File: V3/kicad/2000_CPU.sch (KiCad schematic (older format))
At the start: 18 parts, among them J1 Conn_01x08_Male, U2000 Z8-L180-S180-180-PLCC-68, U2101 GAL16V8, U2102 14.7456 MHz

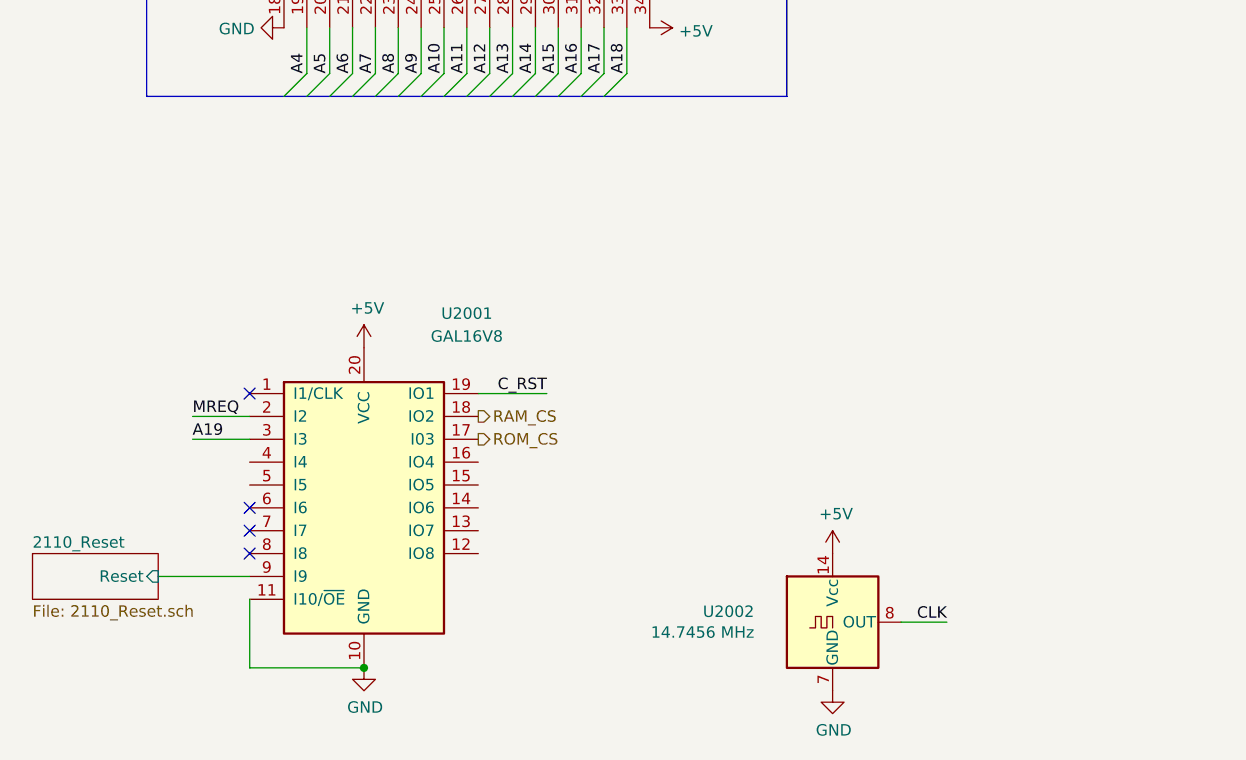
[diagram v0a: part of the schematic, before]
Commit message: Replace reset with simpler circuit
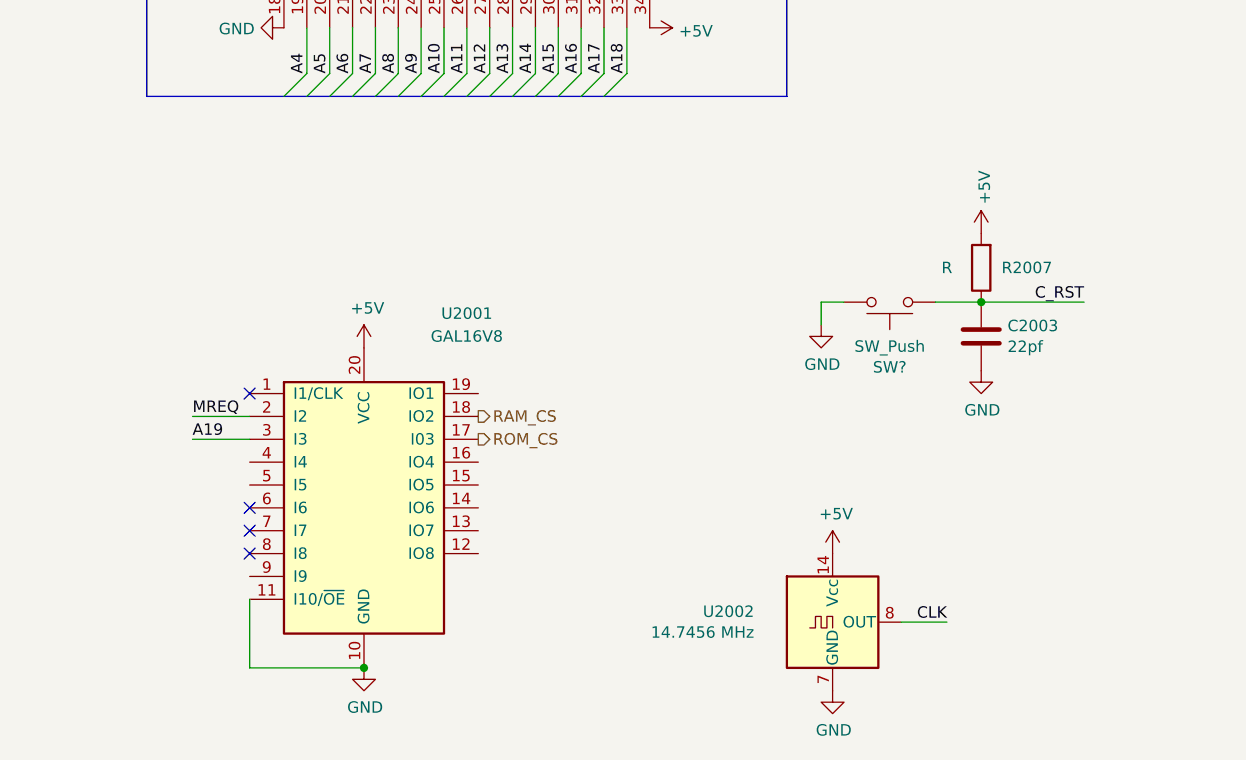
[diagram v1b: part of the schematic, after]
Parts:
- added C2003: 22pf, Capacitor_SMD:C_1206_3216Metric, symbol Device:C
- added R2007: R, Resistor_SMD:R_1206_3216Metric, symbol Device:R
- added SW?: SW_Push, Button_Switch_THT:SW_PUSH_6mm, symbol Switch:SW_Push
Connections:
- net +5V: now also R2007.2
- net C_RST: now also C2003.1, R2007.1, SW?.1; no longer U2101.19 (IO1)
- net GND: now also C2003.2, SW?.2
- net 2110_Reset/Reset: no longer names the net of U2101.9 (I9)
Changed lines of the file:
@@
 $Descr A4 11693 8268
 encoding utf-8
-Sheet 3 5
+Sheet 3 4
 Title ""
 Date ""
@@
 Text HLabel 3300 5700 2    50   Output ~ 0
 RAM_CS
-$Sheet
-S 1350 6300 550  200
-U 62512FB8
-F0 "2110_Reset" 50
-F1 "2110_Reset.sch" 50
-F2 "Reset" I R 1900 6400 50
-$EndSheet
 $Comp
 L Oscillator:ACO-xxxMHz X?
@@
 Text Label 3550 1250 3    50   ~ 0
 CKS
-Text Label 3600 5600 2    50   ~ 0
-C_RST
-Wire Wire Line
-	3300 5600 3600 5600
 $Comp
 L Device:C C?
@@
 Wire Wire Line
 	5150 6600 5350 6600
-Wire Wire Line
-	1900 6400 2300 6400
 Text Label 1950 2200 2    50   ~ 0
 CLK
@@
 Text Label 6750 4750 0    50   ~ 0
 SD_CD
+$Comp
+L Switch:SW_Push SW?
+U 1 1 6545E409
+P 5100 5200
+AR Path="/6545E409" Ref="SW?"  Part="1"
+AR Path="/62497D60/6545E409" Ref="SW?"  Part="1"
+AR Path="/61D852D7/6545E409" Ref="SW?"  Part="1"
+AR Path="/6191B6A2/624CF3AF/6545E409" Ref="SW?"  Part="1"
+AR Path="/6191B6A2/61EBDADB/62512FB8/6545E409" Ref="SW?"  Part="1"
+AR Path="/63A83936/62512FB8/6545E409" Ref="SW?"  Part="1"
+AR Path="/63A83936/6545E409" Ref="SW?"  Part="1"
+F 0 "SW?" H 5100 5485 50  0000 C CNN
+F 1 "SW_Push" H 5100 5394 50  0000 C CNN
+F 2 "Button_Switch_THT:SW_PUSH_6mm" H 5100 5400 50  0001 C CNN
+F 3 "~" H 5100 5400 50  0001 C CNN
+	1    5100 5200
+	-1   0    0    1
+$EndComp
+$Comp
+L Device:R R?
+U 1 1 6546AA6A
+P 5500 5050
+AR Path="/6191B6A2/61EBDADB/6546AA6A" Ref="R?"  Part="1"
+AR Path="/63A83936/6546AA6A" Ref="R2007"  Part="1"
+F 0 "R2007" H 5300 5050 50  0000 C CNN
+F 1 "R" H 5650 5050 50  0000 C CNN
+F 2 "Resistor_SMD:R_1206_3216Metric" V 5430 5050 50  0001 C CNN
+F 3 "~" H 5500 5050 50  0001 C CNN
+	1    5500 5050
+	-1   0    0    1
+$EndComp
+$Comp
+L power:+5V #PWR?
+U 1 1 6546C304
+P 5500 4900
+AR Path="/6191B6A2/61EBDADB/6546C304" Ref="#PWR?"  Part="1"
+AR Path="/63A83936/6546C304" Ref="#PWR?"  Part="1"
+F 0 "#PWR?" H 5500 4750 50  0001 C CNN
+F 1 "+5V" V 5515 5028 50  0000 L CNN
+F 2 "" H 5500 4900 50  0001 C CNN
+F 3 "" H 5500 4900 50  0001 C CNN
+	1    5500 4900
+	1    0    0    -1
+$EndComp
+Text Label 5950 5200 2    50   ~ 0
+C_RST
+Wire Wire Line
+	5500 5200 5950 5200
+Wire Wire Line
+	4900 5200 4800 5200
+Wire Wire Line
+	4800 5200 4800 5300
+$Comp
+L power:GND #PWR?
+U 1 1 6547BF82
+P 4800 5300
+F 0 "#PWR?" H 4800 5050 50  0001 C CNN
+F 1 "GND" H 4805 5127 50  0000 C CNN
+F 2 "" H 4800 5300 50  0001 C CNN
+F 3 "" H 4800 5300 50  0001 C CNN
+	1    4800 5300
+	1    0    0    -1
+$EndComp
+$Comp
+L Device:C C?
+U 1 1 65481B20
+P 5500 5350
+AR Path="/6195D2C9/65481B20" Ref="C?"  Part="1"
+AR Path="/6191B6A2/61F28B7D/65481B20" Ref="C?"  Part="1"
+AR Path="/6191B6A2/61EBDADB/65481B20" Ref="C?"  Part="1"
+AR Path="/63A83936/65481B20" Ref="C2003"  Part="1"
+F 0 "C2003" H 5615 5396 50  0000 L CNN
+F 1 "22pf" H 5615 5305 50  0000 L CNN
+F 2 "Capacitor_SMD:C_1206_3216Metric" H 5538 5200 50  0001 C CNN
+F 3 "~" H 5500 5350 50  0001 C CNN
+	1    5500 5350
+	1    0    0    -1
+$EndComp
+$Comp
+L power:GND #PWR?
+U 1 1 65481B26
+P 5500 5500
+AR Path="/65481B26" Ref="#PWR?"  Part="1"
+AR Path="/62497D60/65481B26" Ref="#PWR?"  Part="1"
+AR Path="/61D852D7/65481B26" Ref="#PWR?"  Part="1"
+AR Path="/6195D2C9/65481B26" Ref="#PWR?"  Part="1"
+AR Path="/6191B6A2/61F28B7D/65481B26" Ref="#PWR?"  Part="1"
+AR Path="/6191B6A2/61EBDADB/65481B26" Ref="#PWR?"  Part="1"
+AR Path="/63A83936/65481B26" Ref="#PWR?"  Part="1"
+F 0 "#PWR?" H 5500 5250 50  0001 C CNN
+F 1 "GND" H 5505 5327 50  0000 C CNN
+F 2 "" H 5500 5500 50  0001 C CNN
+F 3 "" H 5500 5500 50  0001 C CNN
+	1    5500 5500
+	1    0    0    -1
+$EndComp
+Connection ~ 5500 5200
+Wire Wire Line
+	5300 5200 5500 5200
 Wire Bus Line
 	1850 3200 1850 4300

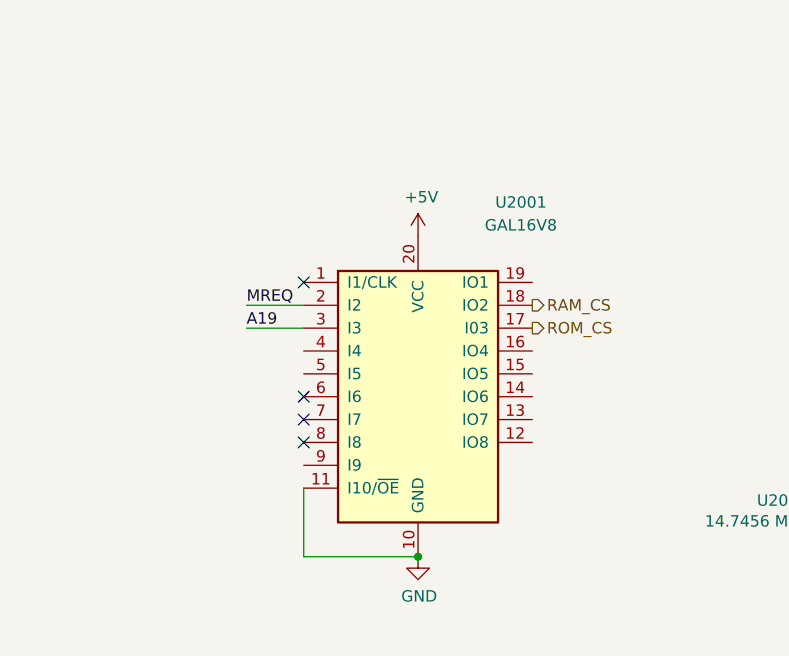
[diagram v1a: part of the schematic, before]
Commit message: replace GAL with 74 series logic
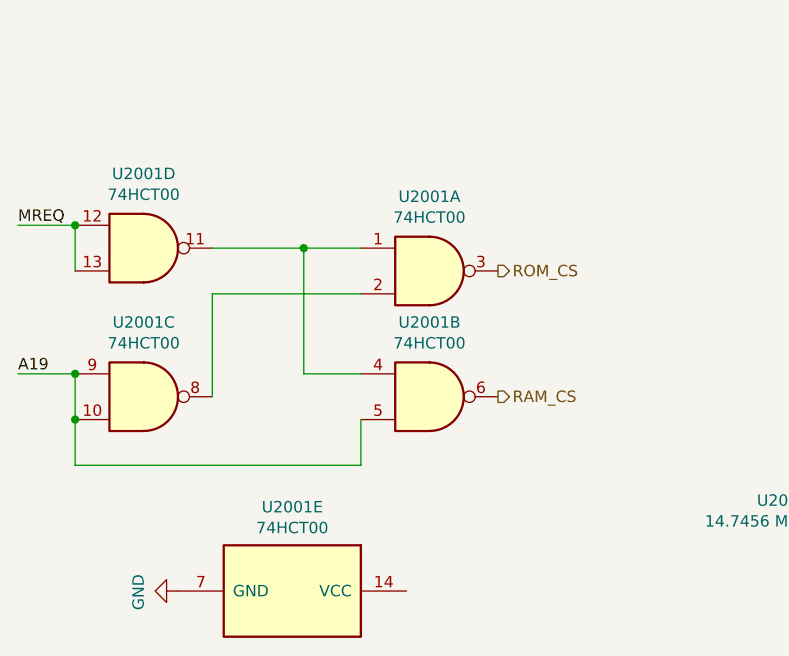
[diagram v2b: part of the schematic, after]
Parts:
- removed U2101: GAL16V8, Package_DIP:DIP-20_W7.62mm_Socket_LongPads, symbol Logic_Programmable:GAL16V8
- added U2001: 74HCT00, symbol 74xx:74HCT00
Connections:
- net A19: now also U2001.10, U2001.5, U2001.9
- net GND: now also U2001.7 (GND)
- net MREQ: now also U2001.12, U2001.13
- net RAM_CS: now also U2001.6
- net ROM_CS: now also U2001.3
- new net: U2001.1, U2001.11, U2001.4
- new net: U2001.2, U2001.8
- no-connect marks 5 -> 1
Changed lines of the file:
@@
 Text Label 4550 3600 2    50   ~ 0
 A19
-$Comp
-L power:GND #PWR?
-U 1 1 624D98DF
-P 2800 6800
-AR Path="/624D98DF" Ref="#PWR?"  Part="1"
-AR Path="/6191B6A2/624D98DF" Ref="#PWR?"  Part="1"
-AR Path="/6191B6A2/61F0BDAE/624D98DF" Ref="#PWR?"  Part="1"
-AR Path="/6195D2C9/624D98DF" Ref="#PWR?"  Part="1"
-AR Path="/6191B6A2/61EBDADB/624D98DF" Ref="#PWR0101"  Part="1"
-AR Path="/63A83936/624D98DF" Ref="#PWR0103"  Part="1"
-F 0 "#PWR0103" H 2800 6550 50  0001 C CNN
-F 1 "GND" H 2805 6627 50  0000 C CNN
-F 2 "" H 2800 6800 50  0001 C CNN
-F 3 "" H 2800 6800 50  0001 C CNN
-	1    2800 6800
-	1    0    0    -1
-$EndComp
-$Comp
-L power:+5V #PWR?
-U 1 1 624D98F5
-P 2800 5400
-AR Path="/6195D2C9/624D98F5" Ref="#PWR?"  Part="1"
-AR Path="/6191B6A2/624D98F5" Ref="#PWR?"  Part="1"
-AR Path="/6191B6A2/61EBDADB/624D98F5" Ref="#PWR0102"  Part="1"
-AR Path="/63A83936/624D98F5" Ref="#PWR0104"  Part="1"
-F 0 "#PWR0104" H 2800 5250 50  0001 C CNN
-F 1 "+5V" H 2815 5573 50  0000 C CNN
-F 2 "" H 2800 5400 50  0001 C CNN
-F 3 "" H 2800 5400 50  0001 C CNN
-	1    2800 5400
-	1    0    0    -1
-$EndComp
-Wire Wire Line
-	2300 5700 2050 5700
-Text Label 2050 5700 0    50   ~ 0
+Text Label 1050 5350 0    50   ~ 0
 MREQ
-Text HLabel 3300 5800 2    50   Output ~ 0
+Text HLabel 3150 5550 2    50   Output ~ 0
 ROM_CS
-Text Label 2050 5800 0    50   ~ 0
-A19
-Text HLabel 3300 5700 2    50   Output ~ 0
+Text HLabel 3150 6100 2    50   Output ~ 0
 RAM_CS
 $Comp
@@
 Text Label 2950 1250 3    50   ~ 0
 MREQ
-$Comp
-L Logic_Programmable:GAL16V8 U?
-U 1 1 624D98D9
-P 2800 6100
-AR Path="/624D98D9" Ref="U?"  Part="1"
-AR Path="/6191B6A2/624D98D9" Ref="U?"  Part="1"
-AR Path="/6191B6A2/61F0BDAE/624D98D9" Ref="U?"  Part="1"
-AR Path="/6195D2C9/624D98D9" Ref="U?"  Part="1"
-AR Path="/6191B6A2/61EBDADB/624D98D9" Ref="U2101"  Part="1"
-AR Path="/63A83936/624D98D9" Ref="U2001"  Part="1"
-F 0 "U2001" H 3250 6950 50  0000 C CNN
-F 1 "GAL16V8" H 3250 6850 50  0000 C CNN
-F 2 "Package_DIP:DIP-20_W7.62mm_Socket_LongPads" H 2800 6100 50  0001 C CNN
-F 3 "" H 2800 6100 50  0001 C CNN
-	1    2800 6100
-	1    0    0    -1
-$EndComp
 Wire Wire Line
 	2150 3100 1850 3100
@@
 	1    0    0    -1
 $EndComp
-Wire Wire Line
-	2050 5800 2300 5800
 Text HLabel 4750 3500 2    50   BiDi ~ 0
 D[0..7]
@@
 Text HLabel 2650 1250 1    50   Output ~ 0
 WR
-NoConn ~ 2300 6200
-NoConn ~ 2300 6300
-Wire Wire Line
-	2300 6500 2300 6800
-Wire Wire Line
-	2300 6800 2800 6800
-Connection ~ 2800 6800
 Text Label 4650 2600 2    50   ~ 0
 RTS0
 Wire Wire Line
 	4650 2600 4350 2600
-NoConn ~ 2300 5600
 $Comp
 L Device:LED D2102/ST1
@@
 	0    -1   -1   0
 $EndComp
-NoConn ~ 2300 6100
 Wire Wire Line
 	2150 3200 1950 3200
@@
 Wire Wire Line
 	5300 5200 5500 5200
+$Comp
+L 74xx:74HCT00 U2001
+U 1 1 6548B5B9
+P 2850 5550
+F 0 "U2001" H 2850 5875 50  0000 C CNN
+F 1 "74HCT00" H 2850 5784 50  0000 C CNN
+F 2 "" H 2850 5550 50  0001 C CNN
+F 3 "http://www.ti.com/lit/gpn/sn74hct00" H 2850 5550 50  0001 C CNN
+	1    2850 5550
+	1    0    0    -1
+$EndComp
+$Comp
+L 74xx:74HCT00 U2001
+U 2 1 6548F371
+P 2850 6100
+F 0 "U2001" H 2850 6425 50  0000 C CNN
+F 1 "74HCT00" H 2850 6334 50  0000 C CNN
+F 2 "" H 2850 6100 50  0001 C CNN
+F 3 "http://www.ti.com/lit/gpn/sn74hct00" H 2850 6100 50  0001 C CNN
+	2    2850 6100
+	1    0    0    -1
+$EndComp
+$Comp
+L 74xx:74HCT00 U2001
+U 3 1 65490F1D
+P 1600 6100
+F 0 "U2001" H 1600 6425 50  0000 C CNN
+F 1 "74HCT00" H 1600 6334 50  0000 C CNN
+F 2 "" H 1600 6100 50  0001 C CNN
+F 3 "http://www.ti.com/lit/gpn/sn74hct00" H 1600 6100 50  0001 C CNN
+	3    1600 6100
+	1    0    0    -1
+$EndComp
+$Comp
+L 74xx:74HCT00 U2001
+U 5 1 65493A9A
+P 2250 6950
+F 0 "U2001" V 1883 6950 50  0000 C CNN
+F 1 "74HCT00" V 1974 6950 50  0000 C CNN
+F 2 "" H 2250 6950 50  0001 C CNN
+F 3 "http://www.ti.com/lit/gpn/sn74hct00" H 2250 6950 50  0001 C CNN
+	5    2250 6950
+	0    1    1    0
+$EndComp
+Wire Wire Line
+	1050 6000 1300 6000
+Text Label 1050 6000 0    50   ~ 0
+A19
+Wire Wire Line
+	1300 6000 1300 6200
+Connection ~ 1300 6000
+Wire Wire Line
+	1900 5450 2300 5450
+Wire Wire Line
+	1900 6100 1900 5650
+Wire Wire Line
+	1900 5650 2550 5650
+Wire Wire Line
+	1300 6200 1300 6400
+Wire Wire Line
+	1300 6400 2550 6400
+Wire Wire Line
+	2550 6400 2550 6200
+Connection ~ 1300 6200
+Wire Wire Line
+	2300 5450 2300 6000
+Wire Wire Line
+	2300 6000 2550 6000
+Connection ~ 2300 5450
+Wire Wire Line
+	2300 5450 2550 5450
+$Comp
+L power:GND #PWR?
+U 1 1 654D56A5
+P 1750 6950
+AR Path="/654D56A5" Ref="#PWR?"  Part="1"
+AR Path="/62497D60/654D56A5" Ref="#PWR?"  Part="1"
+AR Path="/61D852D7/654D56A5" Ref="#PWR?"  Part="1"
+AR Path="/6195D2C9/654D56A5" Ref="#PWR?"  Part="1"
+AR Path="/6191B6A2/61F28B7D/654D56A5" Ref="#PWR?"  Part="1"
+AR Path="/6191B6A2/61EBDADB/654D56A5" Ref="#PWR?"  Part="1"
+AR Path="/63A83936/654D56A5" Ref="#PWR?"  Part="1"
+F 0 "#PWR?" H 1750 6700 50  0001 C CNN
+F 1 "GND" H 1755 6777 50  0000 C CNN
+F 2 "" H 1750 6950 50  0001 C CNN
+F 3 "" H 1750 6950 50  0001 C CNN
+	1    1750 6950
+	0    1    1    0
+$EndComp
+Connection ~ 1300 5350
+Wire Wire Line
+	1300 5350 1300 5550
+$Comp
+L 74xx:74HCT00 U2001
+U 4 1 65492729
+P 1600 5450
+F 0 "U2001" H 1600 5775 50  0000 C CNN
+F 1 "74HCT00" H 1600 5684 50  0000 C CNN
+F 2 "" H 1600 5450 50  0001 C CNN
+F 3 "http://www.ti.com/lit/gpn/sn74hct00" H 1600 5450 50  0001 C CNN
+	4    1600 5450
+	1    0    0    -1
+$EndComp
+Wire Wire Line
+	1300 5350 1050 5350
 Wire Bus Line
 	1850 3200 1850 4300

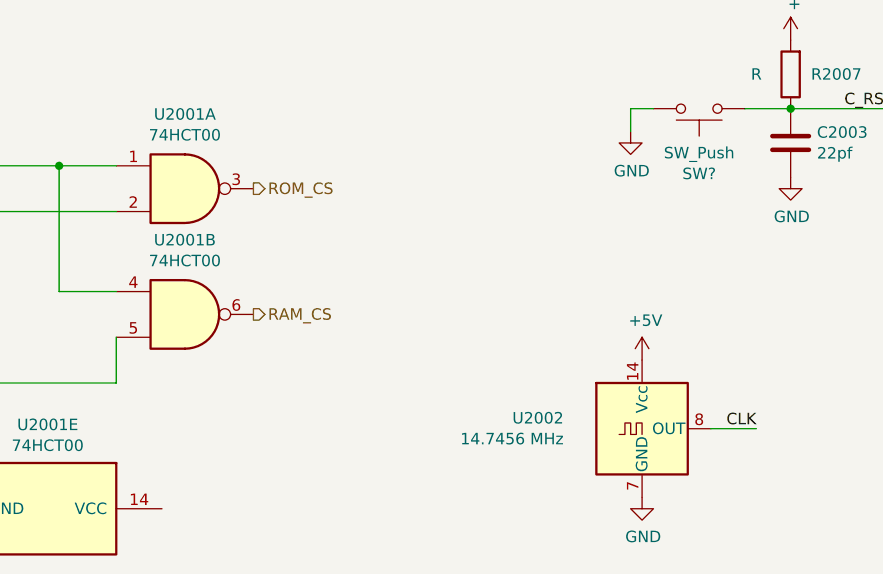
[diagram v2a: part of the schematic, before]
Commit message: rearranged pcb a bit
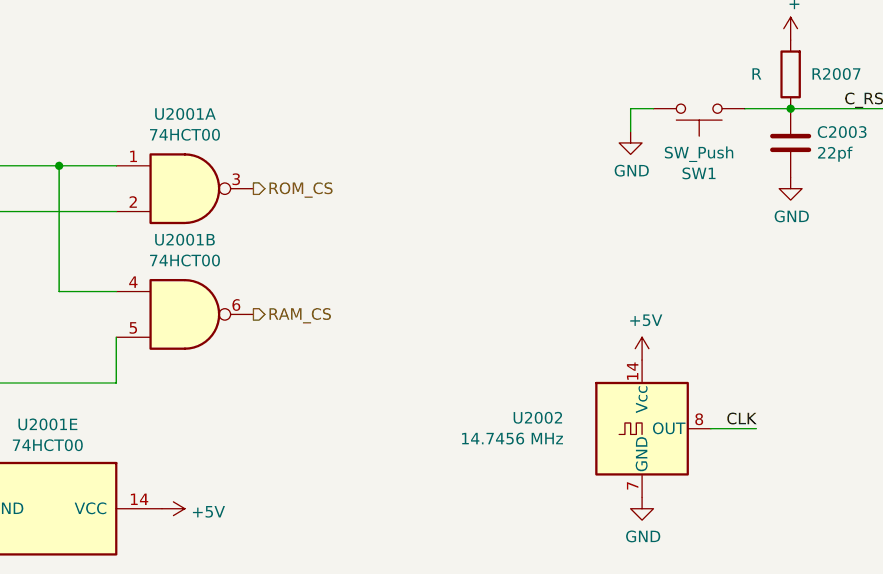
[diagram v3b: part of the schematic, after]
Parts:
- U2001: footprint (none) -> Package_DIP:DIP-14_W7.62mm_Socket_LongPads
- gave numbers to parts that had none: 1
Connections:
- net +5V: now also U2001.14 (VCC)
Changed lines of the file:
@@
 AR Path="/6191B6A2/61EBDADB/62512FB8/6545E409" Ref="SW?"  Part="1"
 AR Path="/63A83936/62512FB8/6545E409" Ref="SW?"  Part="1"
-AR Path="/63A83936/6545E409" Ref="SW?"  Part="1"
-F 0 "SW?" H 5100 5485 50  0000 C CNN
+AR Path="/63A83936/6545E409" Ref="SW1"  Part="1"
+F 0 "SW1" H 5100 5485 50  0000 C CNN
 F 1 "SW_Push" H 5100 5394 50  0000 C CNN
 F 2 "Button_Switch_THT:SW_PUSH_6mm" H 5100 5400 50  0001 C CNN
@@
 P 5500 4900
 AR Path="/6191B6A2/61EBDADB/6546C304" Ref="#PWR?"  Part="1"
-AR Path="/63A83936/6546C304" Ref="#PWR?"  Part="1"
-F 0 "#PWR?" H 5500 4750 50  0001 C CNN
+AR Path="/63A83936/6546C304" Ref="#PWR0103"  Part="1"
+F 0 "#PWR0103" H 5500 4750 50  0001 C CNN
 F 1 "+5V" V 5515 5028 50  0000 L CNN
 F 2 "" H 5500 4900 50  0001 C CNN
@@
 	4800 5200 4800 5300
 $Comp
-L power:GND #PWR?
+L power:GND #PWR0104
 U 1 1 6547BF82
 P 4800 5300
-F 0 "#PWR?" H 4800 5050 50  0001 C CNN
+F 0 "#PWR0104" H 4800 5050 50  0001 C CNN
 F 1 "GND" H 4805 5127 50  0000 C CNN
 F 2 "" H 4800 5300 50  0001 C CNN
@@
 AR Path="/6191B6A2/61F28B7D/65481B26" Ref="#PWR?"  Part="1"
 AR Path="/6191B6A2/61EBDADB/65481B26" Ref="#PWR?"  Part="1"
-AR Path="/63A83936/65481B26" Ref="#PWR?"  Part="1"
-F 0 "#PWR?" H 5500 5250 50  0001 C CNN
+AR Path="/63A83936/65481B26" Ref="#PWR0105"  Part="1"
+F 0 "#PWR0105" H 5500 5250 50  0001 C CNN
 F 1 "GND" H 5505 5327 50  0000 C CNN
 F 2 "" H 5500 5500 50  0001 C CNN
@@
 F 0 "U2001" H 2850 5875 50  0000 C CNN
 F 1 "74HCT00" H 2850 5784 50  0000 C CNN
-F 2 "" H 2850 5550 50  0001 C CNN
+F 2 "Package_DIP:DIP-14_W7.62mm_Socket_LongPads" H 2850 5550 50  0001 C CNN
 F 3 "http://www.ti.com/lit/gpn/sn74hct00" H 2850 5550 50  0001 C CNN
 	1    2850 5550
@@
 F 0 "U2001" H 2850 6425 50  0000 C CNN
 F 1 "74HCT00" H 2850 6334 50  0000 C CNN
-F 2 "" H 2850 6100 50  0001 C CNN
+F 2 "Package_DIP:DIP-14_W7.62mm_Socket_LongPads" H 2850 6100 50  0001 C CNN
 F 3 "http://www.ti.com/lit/gpn/sn74hct00" H 2850 6100 50  0001 C CNN
 	2    2850 6100
@@
 F 0 "U2001" H 1600 6425 50  0000 C CNN
 F 1 "74HCT00" H 1600 6334 50  0000 C CNN
-F 2 "" H 1600 6100 50  0001 C CNN
+F 2 "Package_DIP:DIP-14_W7.62mm_Socket_LongPads" H 1600 6100 50  0001 C CNN
 F 3 "http://www.ti.com/lit/gpn/sn74hct00" H 1600 6100 50  0001 C CNN
 	3    1600 6100
@@
 F 0 "U2001" V 1883 6950 50  0000 C CNN
 F 1 "74HCT00" V 1974 6950 50  0000 C CNN
-F 2 "" H 2250 6950 50  0001 C CNN
+F 2 "Package_DIP:DIP-14_W7.62mm_Socket_LongPads" H 2250 6950 50  0001 C CNN
 F 3 "http://www.ti.com/lit/gpn/sn74hct00" H 2250 6950 50  0001 C CNN
 	5    2250 6950
@@
 AR Path="/6191B6A2/61F28B7D/654D56A5" Ref="#PWR?"  Part="1"
 AR Path="/6191B6A2/61EBDADB/654D56A5" Ref="#PWR?"  Part="1"
-AR Path="/63A83936/654D56A5" Ref="#PWR?"  Part="1"
-F 0 "#PWR?" H 1750 6700 50  0001 C CNN
+AR Path="/63A83936/654D56A5" Ref="#PWR0106"  Part="1"
+F 0 "#PWR0106" H 1750 6700 50  0001 C CNN
 F 1 "GND" H 1755 6777 50  0000 C CNN
 F 2 "" H 1750 6950 50  0001 C CNN
@@
 F 0 "U2001" H 1600 5775 50  0000 C CNN
 F 1 "74HCT00" H 1600 5684 50  0000 C CNN
-F 2 "" H 1600 5450 50  0001 C CNN
+F 2 "Package_DIP:DIP-14_W7.62mm_Socket_LongPads" H 1600 5450 50  0001 C CNN
 F 3 "http://www.ti.com/lit/gpn/sn74hct00" H 1600 5450 50  0001 C CNN
 	4    1600 5450
@@
 Wire Wire Line
 	1300 5350 1050 5350
+$Comp
+L power:+5V #PWR?
+U 1 1 65505CDB
+P 2750 6950
+AR Path="/6191B6A2/61EBDADB/65505CDB" Ref="#PWR?"  Part="1"
+AR Path="/63A83936/65505CDB" Ref="#PWR?"  Part="1"
+F 0 "#PWR?" H 2750 6800 50  0001 C CNN
+F 1 "+5V" V 2765 7078 50  0000 L CNN
+F 2 "" H 2750 6950 50  0001 C CNN
+F 3 "" H 2750 6950 50  0001 C CNN
+	1    2750 6950
+	0    1    1    0
+$EndComp
 Wire Bus Line
 	1850 3200 1850 4300
